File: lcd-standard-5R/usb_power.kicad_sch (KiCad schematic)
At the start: 5 parts, among them J4 USB_C_Receptacle_USB2.0_16P

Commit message: Slight changes
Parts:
- C8: JLCPCB Part # (none) -> C1779
- C9: footprint Capacitor_SMD:C_0603_1608Metric -> Capacitor_SMD:C_0402_1005Metric; JLCPCB Part # (none) -> C1525
- J4: JLCPCB Part # (none) -> C963412
- R10, R9: JLCPCB Part # (none) -> C25905
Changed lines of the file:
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@@
+			)
+		)
+		(property "JLCPCB Part #" "C1779"
+			(at 162.56 60.96 0)
+			(effects
+				(font
+					(size 1.27 1.27)
+				)
+				(hide yes)
 			)
 		)
@@
 			)
 		)
+		(property "JLCPCB Part #" "C25905"
+			(at 180.34 76.2 0)
+			(effects
+				(font
+					(size 1.27 1.27)
+				)
+				(hide yes)
+			)
+		)
 		(pin "2"
 		)
@@
 			)
 		)
-		(property "Footprint" "Capacitor_SMD:C_0603_1608Metric"
+		(property "Footprint" "Capacitor_SMD:C_0402_1005Metric"
 			(at 172.72 60.96 0)
 			(effects
@@
 		)
 		(property "Description" "Unpolarized capacitor, small symbol"
+			(at 172.72 60.96 0)
+			(effects
+				(font
+					(size 1.27 1.27)
+				)
+				(hide yes)
+			)
+		)
+		(property "JLCPCB Part #" "C1525"
 			(at 172.72 60.96 0)
 			(effects
@@
 			)
 		)
+		(property "JLCPCB Part #" "C25905"
+			(at 180.34 78.74 0)
+			(effects
+				(font
+					(size 1.27 1.27)
+				)
+				(hide yes)
+			)
+		)
 		(pin "2"
 		)
@@
 			(at 203.2 86.36 0)
 			(effects
+				(font
+					(size 1.27 1.27)
+				)
+				(hide yes)
+			)
+		)
+		(property "JLCPCB Part #" "C963412"
+			(at 203.2 86.36 0)
+			(effects

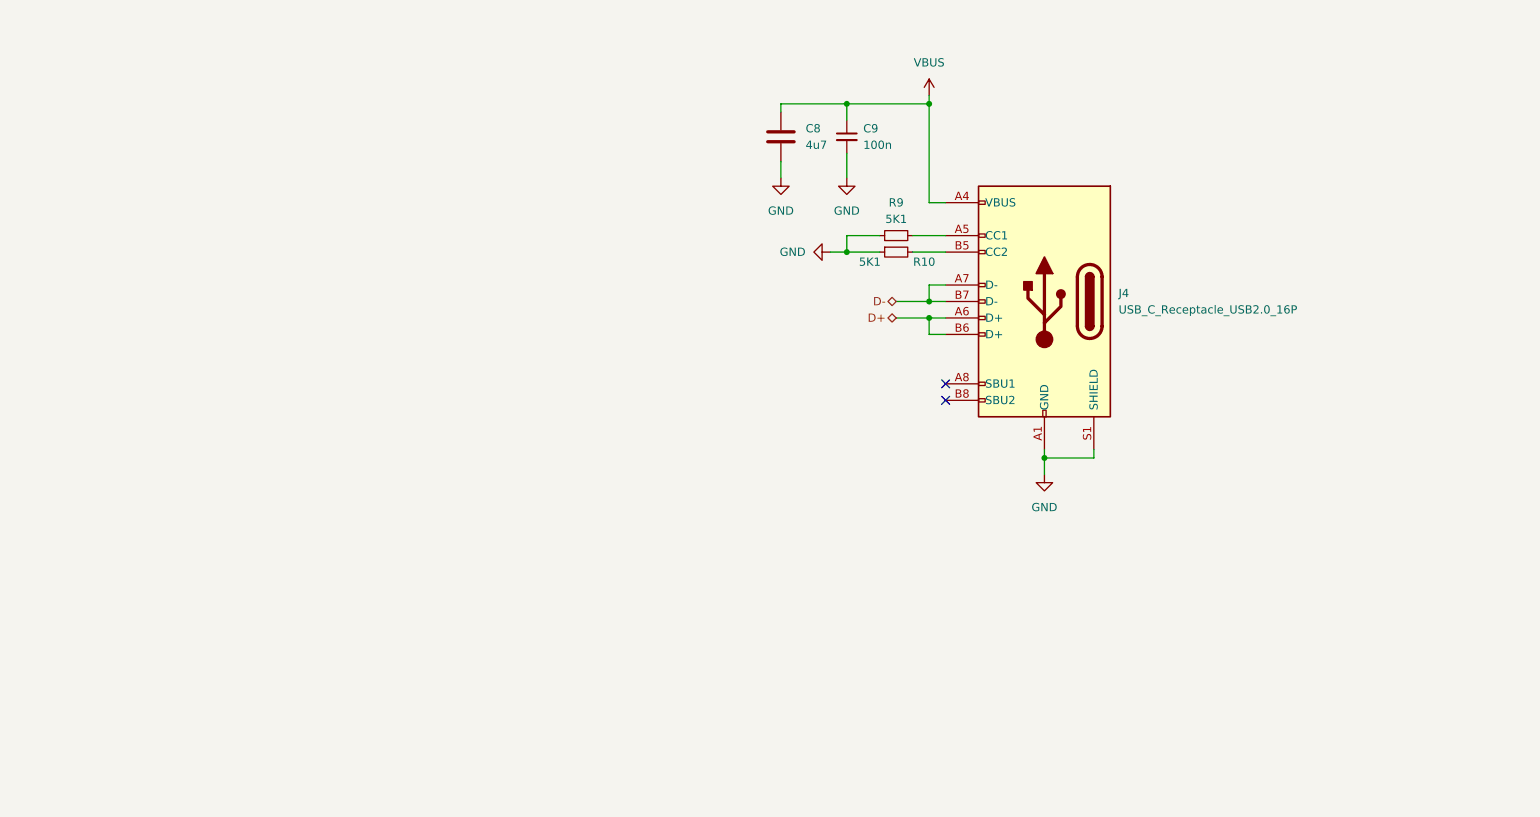
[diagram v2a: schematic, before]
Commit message: Change LCD 5R to onboard MCU, cause separate boards are too expensive
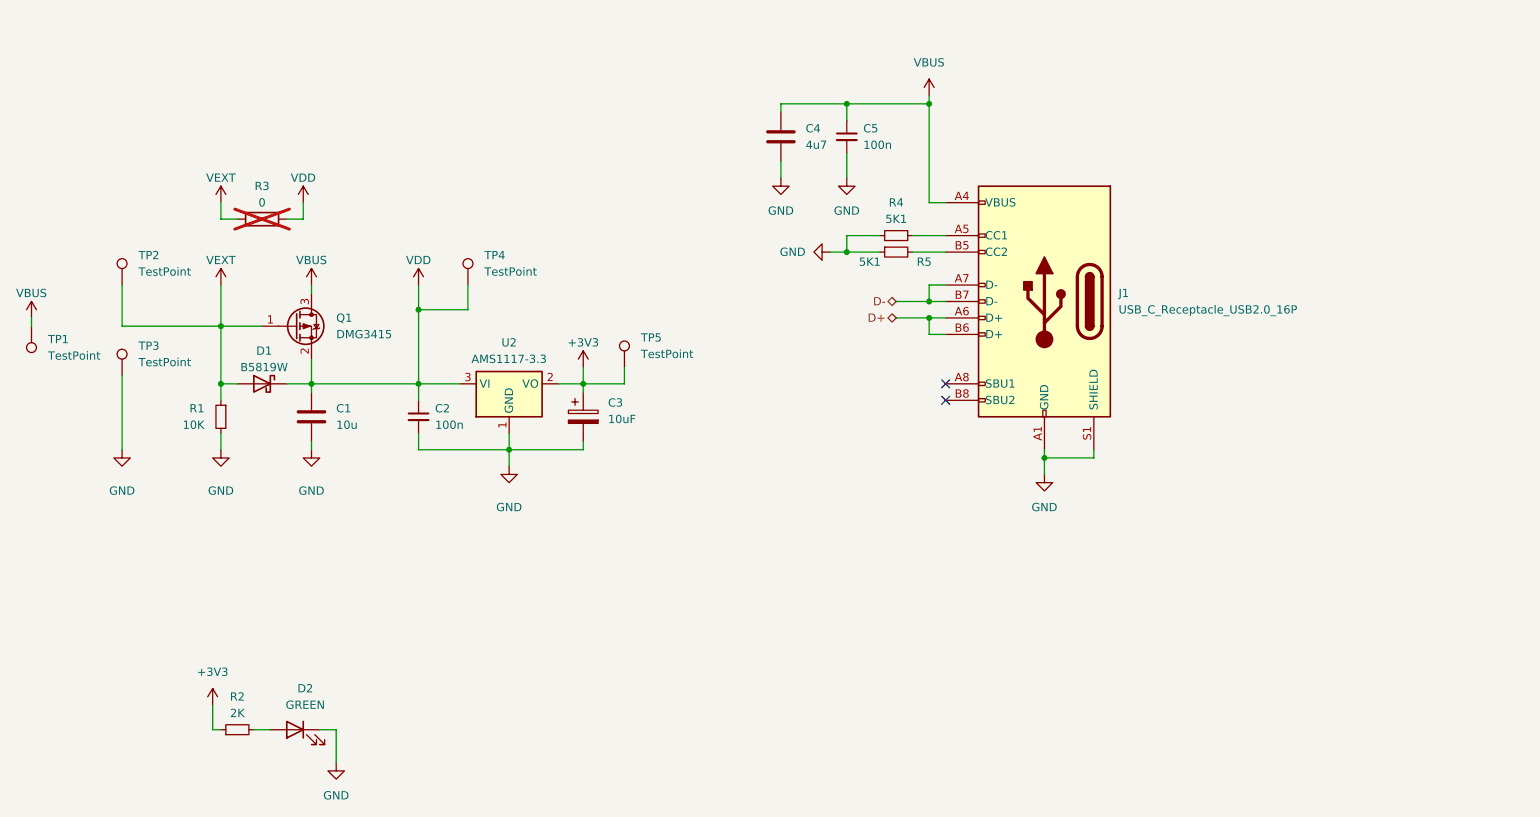
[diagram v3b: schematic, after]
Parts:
- added C1: 10u, Capacitor_SMD:C_0805_2012Metric, symbol Device:C
- added C2: 100n, Capacitor_SMD:C_0402_1005Metric, symbol Device:C_Small
- added C3: 10uF, Capacitor_Tantalum_SMD:CP_EIA-3216-18_Kemet-A, symbol Device:C_Polarized
- added D1: B5819W, Diode_SMD:D_SOD-123, symbol Diode:MBR0540
- added D2: GREEN, LED_SMD:LED_0805_2012Metric, symbol Device:LED
- added Q1: DMG3415, Package_TO_SOT_SMD:SOT-23, symbol Transistor_FET:DMG2301L
- added R1: 10K, Resistor_SMD:R_0402_1005Metric, symbol Device:R_Small
- added R2: 2K, Resistor_SMD:R_0402_1005Metric, symbol Device:R_Small
- added R3: 0, Resistor_SMD:R_1206_3216Metric, symbol Device:R
- added TP1, TP2, TP3, TP4, TP5: TestPoint, TestPoint:TestPoint_Pad_D1.0mm, symbol Connector:TestPoint
- added U2: AMS1117-3.3, Package_TO_SOT_SMD:SOT-223-3_TabPin2, symbol Regulator_Linear:AMS1117-3.3
- renumbered C8 to C4, C9 to C5, J4 to J1, R9 to R4, R10 to R5
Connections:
- net GND: now also C1.2, C2.2, C3.2, D2.1 (K), R1.2, TP3.1, U2.1 (GND)
- net VBUS: now also Q1.3 (D), TP1.1
- new net: D2.2 (A), R2.2
- new net +3V3: C3.1, R2.1, TP5.1, U2.2 (VO)
- new net VDD: C1.1, C2.1, D1.1 (K), Q1.2 (S), R3.2, TP4.1, U2.3 (VI)
- new net VEXT: D1.2 (A), Q1.1 (G), R1.1, R3.1, TP2.1

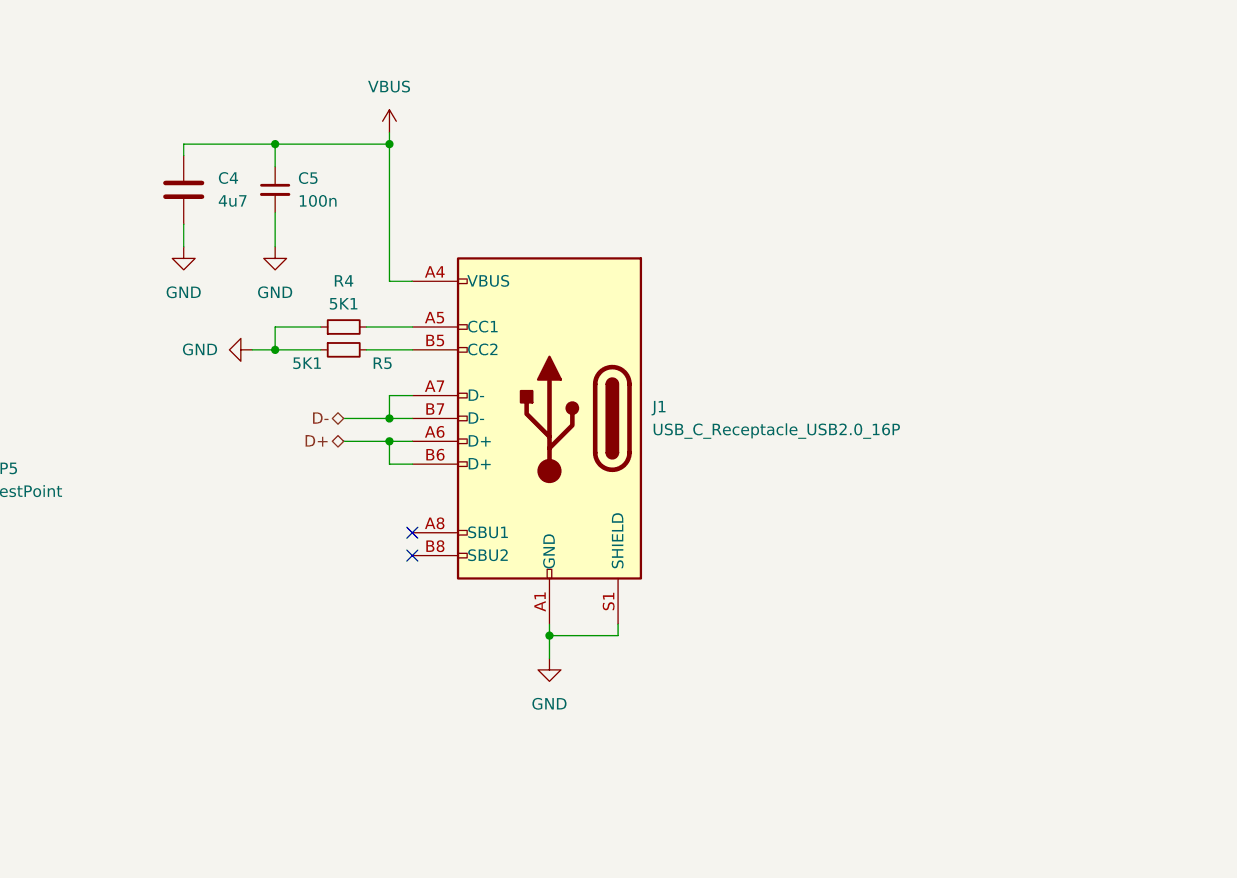
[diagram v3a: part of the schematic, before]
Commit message: Change MCU to STM32H743
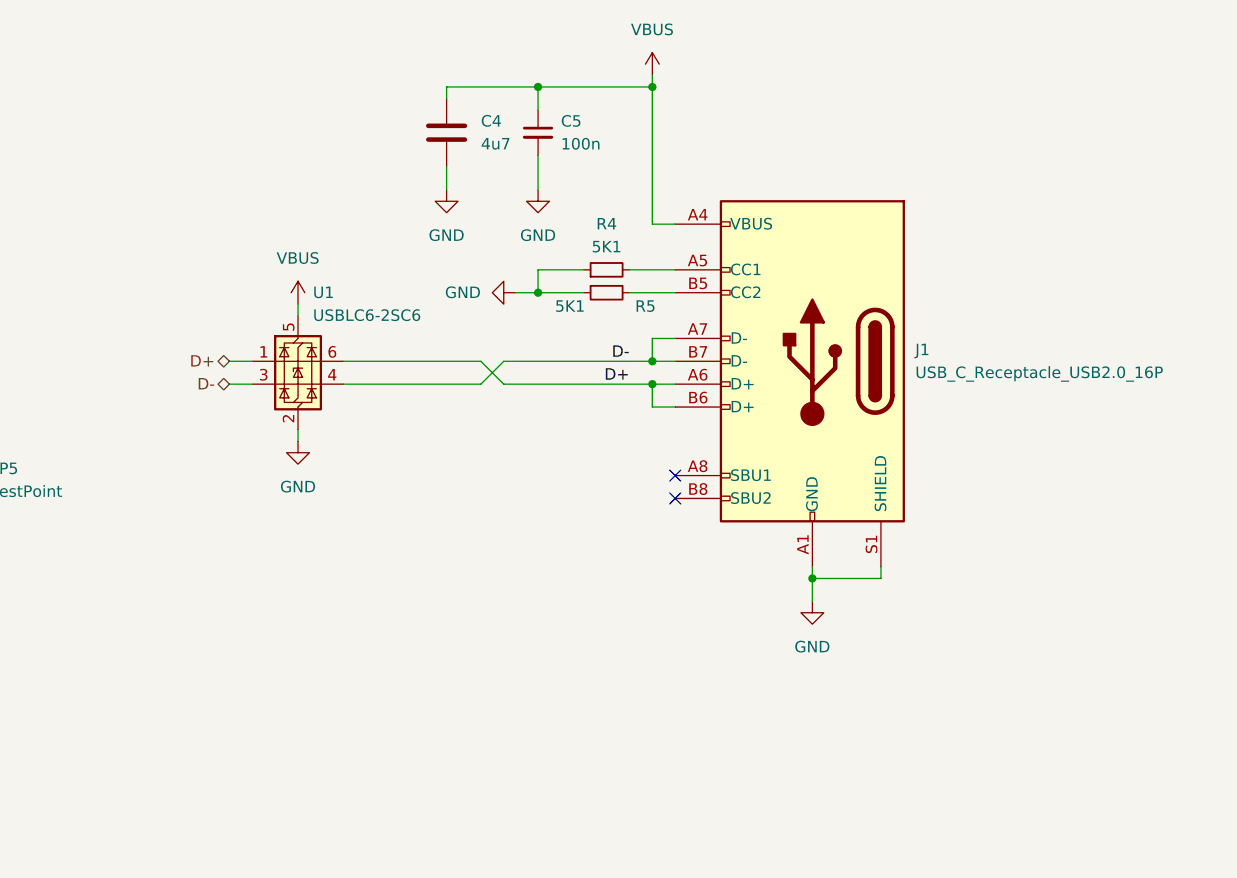
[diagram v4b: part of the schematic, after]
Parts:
- added U1: USBLC6-2SC6, Package_TO_SOT_SMD:SOT-23-6, symbol Power_Protection:USBLC6-2SC6
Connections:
- net D+: now also U1.1 (I/O1), U1.6 (I/O1)
- net D-: now also U1.3 (I/O2), U1.4 (I/O2)
- net GND: now also U1.2 (GND)
- net VBUS: now also U1.5 (VBUS)
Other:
- moved on the sheet: C4, C5, J1, R4, R5

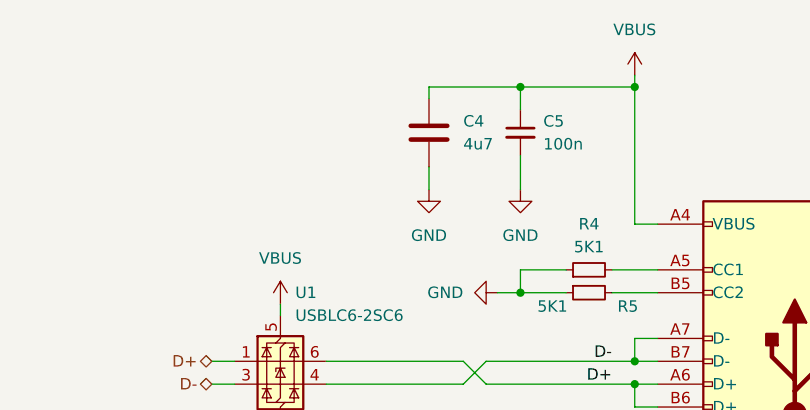
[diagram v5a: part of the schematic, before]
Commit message: Change 10P CTP to omron type
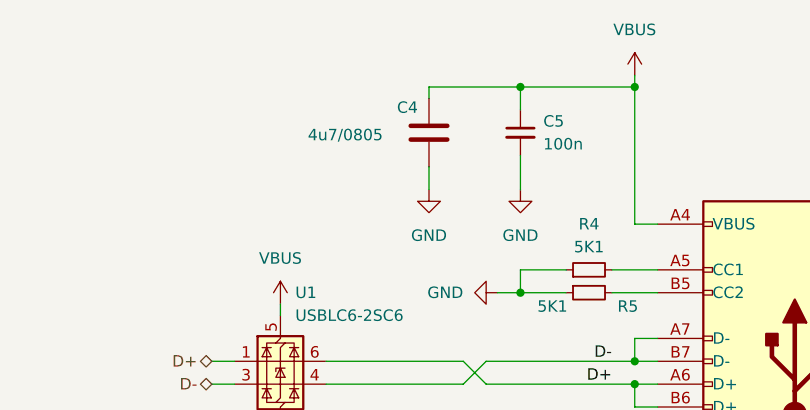
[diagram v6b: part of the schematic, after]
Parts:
- C2, C5: JLCPCB Part # C1525 -> C307331
- C4: value 4u7 -> 4u7/0805
- U1: JLCPCB Part # (none) -> C2827654
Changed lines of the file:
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@@
+			)
+		)
+		(property "JLCPCB Part #" "C2827654"
+			(at 175.26 80.01 0)
+			(effects
+				(font
+					(size 1.27 1.27)
+				)
+				(hide yes)
 			)
 		)
@@
 		(on_board yes)
 		(dnp no)
-		(fields_autoplaced yes)
 		(property "Reference" "C4"
-			(at 195.58 53.3399 0)
-			(effects
-				(font
-					(size 1.27 1.27)
-				)
-				(justify left)
-			)
-		)
-		(property "Value" "4u7"
-			(at 195.58 55.8799 0)
+			(at 188.214 51.816 0)
+			(effects
+				(font
+					(size 1.27 1.27)
+				)
+				(justify left)
+			)
+		)
+		(property "Value" "4u7/0805"
+			(at 178.308 54.864 0)
 			(effects
 				(font
@@
 			)
 		)
-		(property "JLCPCB Part #" "C1525"
+		(property "JLCPCB Part #" "C307331"
 			(at 201.93 54.61 0)
 			(effects
@@
 			)
 		)
-		(property "JLCPCB Part #" "C1525"
+		(property "JLCPCB Part #" "C307331"
 			(at 106.68 104.14 0)
 			(effects

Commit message: Add QSPI Flash trace length matching to 5 inch LCD
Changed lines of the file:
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@@
 (kicad_sch
-	(version 20231120)
+	(version 20250114)
 	(generator "eeschema")
-	(generator_version "8.0")
+	(generator_version "9.0")
 	(paper "A4")
 	(junction
@@
 	(label "D-"
 		(at 212.09 80.01 180)
-		(fields_autoplaced yes)
 		(effects
 			(font
@@
 	(label "D+"
 		(at 212.09 82.55 180)
-		(fields_autoplaced yes)
 		(effects
 			(font
@@
 		(shape bidirectional)
 		(at 167.64 80.01 180)
-		(fields_autoplaced yes)
 		(effects
 			(font
@@
 		(shape bidirectional)
 		(at 167.64 82.55 180)
-		(fields_autoplaced yes)
 		(effects
 			(font
